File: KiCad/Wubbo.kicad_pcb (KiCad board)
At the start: 2 copper layers, 140 x 91.2 mm, 57 parts, among them J1 USB_C_Receptacle, J2 SWD, J3 USB, J4 JST-BATT, J5 USB, Q1 AO3407, Q2 AO3407, SW1 Choc, SW10 Choc, SW11 Choc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

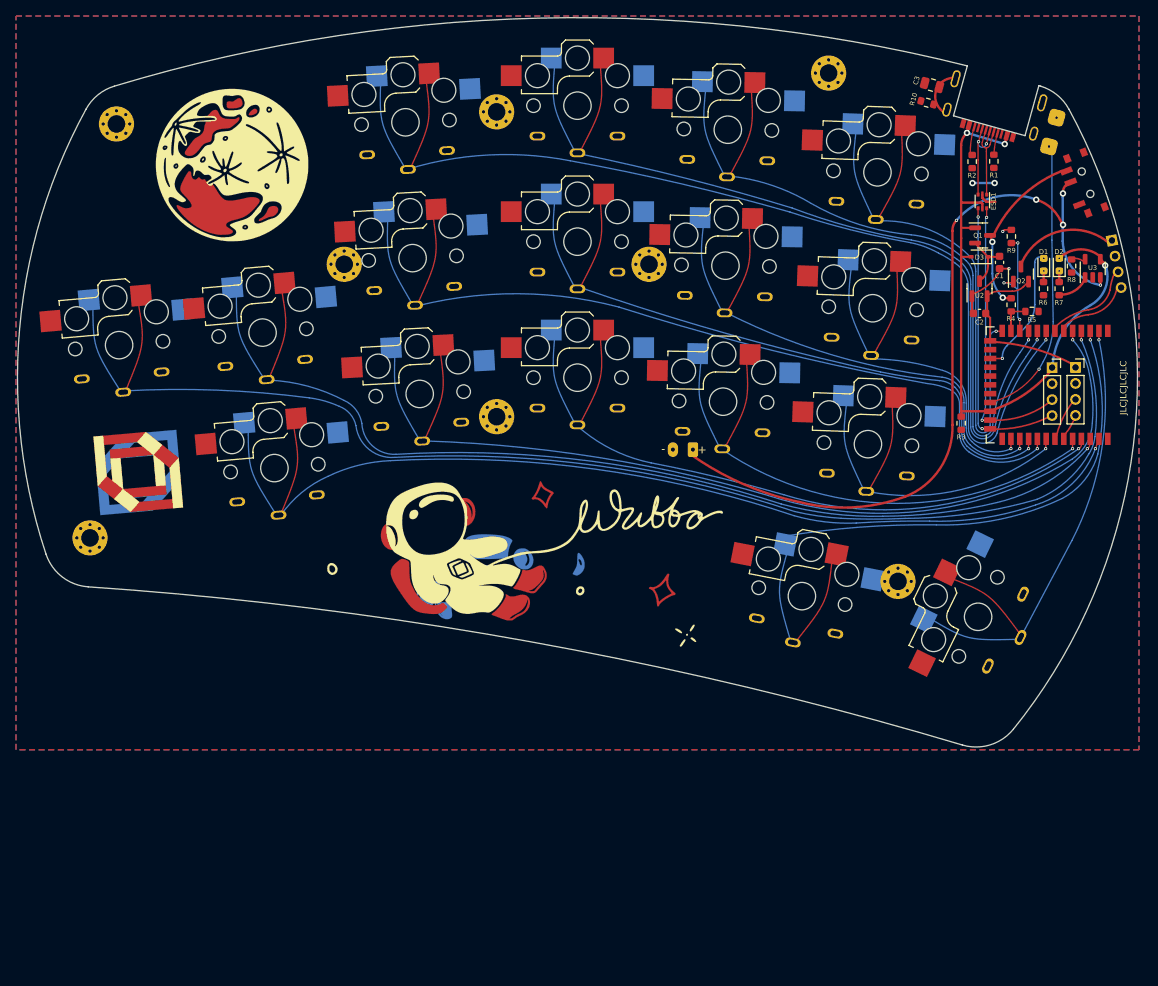
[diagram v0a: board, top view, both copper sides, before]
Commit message: Various modifications to make it 38 keys
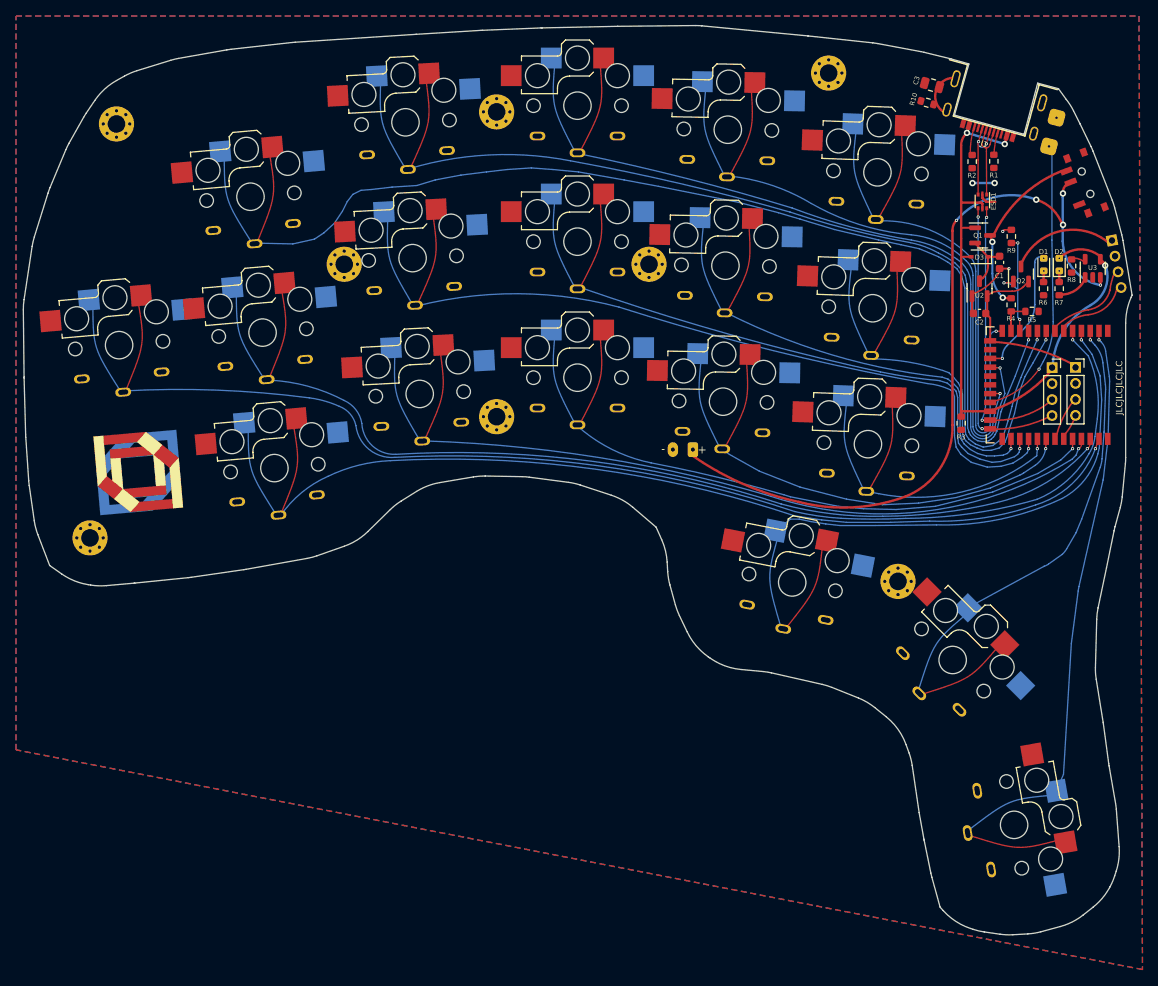
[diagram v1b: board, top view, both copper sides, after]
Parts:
- removed GR3: , kiboard_cache:frontright-2
- removed GR4: , kiboard_cache:frontleft-2
- removed GR5: , kiboard_cache:frontright-1
- removed GR6: , kiboard_cache:frontleft-1
- added SW18: Choc, kiboard_cache:PG13500-reversible, F.Cu at (110.4, 43.0)
- added SW19: Choc, kiboard_cache:PG13500-reversible, F.Cu at (14.9, -35.5)
- J1: footprint USB-C-12-Pin-MidMount -> footprints:USB-C-12-Pin-MidMount
- SW1, SW10, SW11, SW12, SW13, SW14, SW15, SW16, SW17, SW2, SW3, SW4, SW5, SW6, SW7, SW8, SW9: footprint kiboard_cache:combined-choc-reversible -> kiboard_cache:PG13500-reversible
- moved SW17 6.27 mm to (102.7, 22.4), turned to 135 degrees
- moved SW16 2.10 mm to (82.7, 12.7)
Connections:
- R1 pad 1: Net-(J1-PadA5) -> Net-(J1-CC1)
- R2 pad 1: Net-(J1-PadB5) -> Net-(J1-CC2)
- U1 pad 10: SW4 -> SW2
- U1 pad 17: /unconnected-(U1-P0.12) -> SW3
- U1 pad 2: SW17 -> SW18
- U1 pad 20: /unconnected-(U1-P0.19) -> SW4
- U1 pad 26: SW10 -> SW9
- U1 pad 27: SW9 -> SW8
- U1 pad 28: SW8 -> SW7
- U1 pad 29: SW7 -> SW15
- U1 pad 3: SW16 -> SW17
- U1 pad 30: SW15 -> SW14
- U1 pad 33: SW14 -> SW13
- U1 pad 34: SW13 -> SW12
- U1 pad 4: SW1 -> SW16
- U1 pad 5: SW12 -> SW1
- U1 pad 8: SW2 -> SW10
- U1 pad 9: SW3 -> SW19
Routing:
- net SW19: track 0.00 -> 133.4 mm, vias 0 -> 1
- net SW18: track 0.00 -> 58.4 mm, vias 0 -> 1
- net SW12: track 100.0 -> 85.1 mm
- net SW10: track 25.8 -> 39.7 mm
- net SW4: track 68.8 -> 61.3 mm
- net SW3: track 88.2 -> 83.8 mm
- net SW16: track 58.1 -> 62.4 mm
- net Net-(J1-PadB5): track 3.40 -> 0.00 mm
- net Net-(J1-CC2): track 0.00 -> 3.40 mm
- net Net-(J1-PadA5): track 2.73 -> 0.00 mm
- net Net-(J1-CC1): track 0.00 -> 2.73 mm
- net SW17: track 40.5 -> 43.2 mm
- net SW14: track 46.6 -> 45.2 mm
- net SW2: track 110.7 -> 109.9 mm
- net SW1: track 143.0 -> 143.7 mm
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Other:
- board size 140 x 91.2 mm -> 138.6 x 113.7 mm
